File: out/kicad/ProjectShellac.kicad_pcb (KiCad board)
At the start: 4 copper layers, 220 x 140 mm, 259 parts, among them U101 OPA1656, U103 OPA1655, U201 OPA1656, U203 OPA1655, U3001 OPA1612, U3501 OPA1612, U401 OPA1656, U501 OPA1656, U700 OPA1656, U750 OPA1656, U8001 L THAT1646, U9001 R THAT1646

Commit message: AE-074: migrate DR-039 branch-local DC block and reconcile native PCB
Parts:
- TP3004: value L_EQ_RAW -> L_RECOVERY_OUT
- TP3005: value L_EQ_OUT -> L_POST_EQ
- TP3504: value R_EQ_RAW -> R_RECOVERY_OUT
- TP3505: value R_EQ_OUT -> R_POST_EQ
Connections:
- C30060 pad 1: Net-(TP3004-TP) -> Net-(C30060-Pad1)
- C35060 pad 1: Net-(TP3504-TP) -> Net-(C35060-Pad1)
- R30041 pad 1: Net-(TP3004-TP) -> ROOT__POST_EQ_L
- R30060 pad 1: ROOT__POST_EQ_L -> Net-(C30060-Pad1)
- R35041 pad 1: Net-(TP3504-TP) -> ROOT__POST_EQ_R
- R35060 pad 1: ROOT__POST_EQ_R -> Net-(C35060-Pad1)
- TP3004 pad 1: Net-(TP3004-TP) -> ROOT__POST_EQ_L
- TP3504 pad 1: Net-(TP3504-TP) -> ROOT__POST_EQ_R
- U3001 pad 7: Net-(TP3004-TP) -> ROOT__POST_EQ_L
- U3501 pad 7: Net-(TP3504-TP) -> ROOT__POST_EQ_R

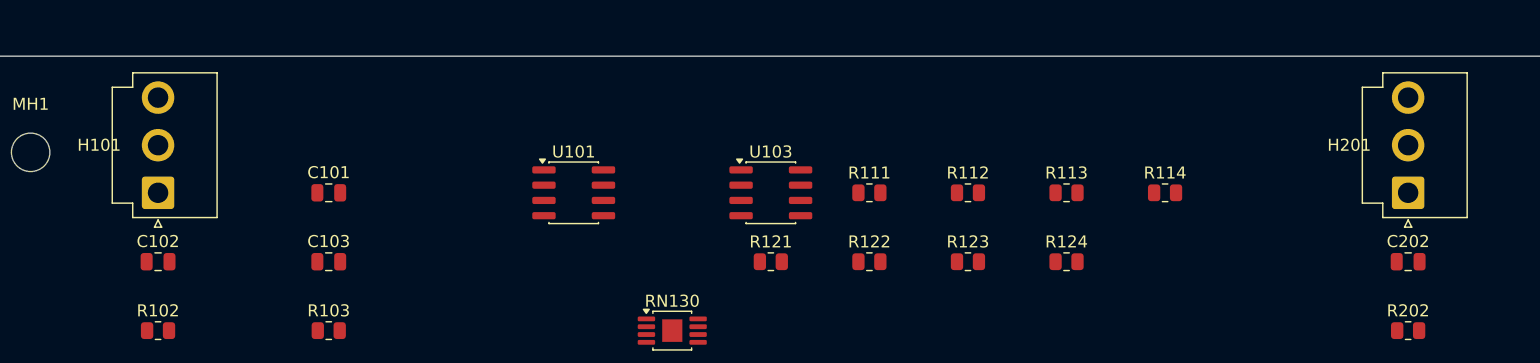
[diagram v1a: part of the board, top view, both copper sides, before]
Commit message: AE-075: close B07 cartridge input harness and Micro-Lock migration
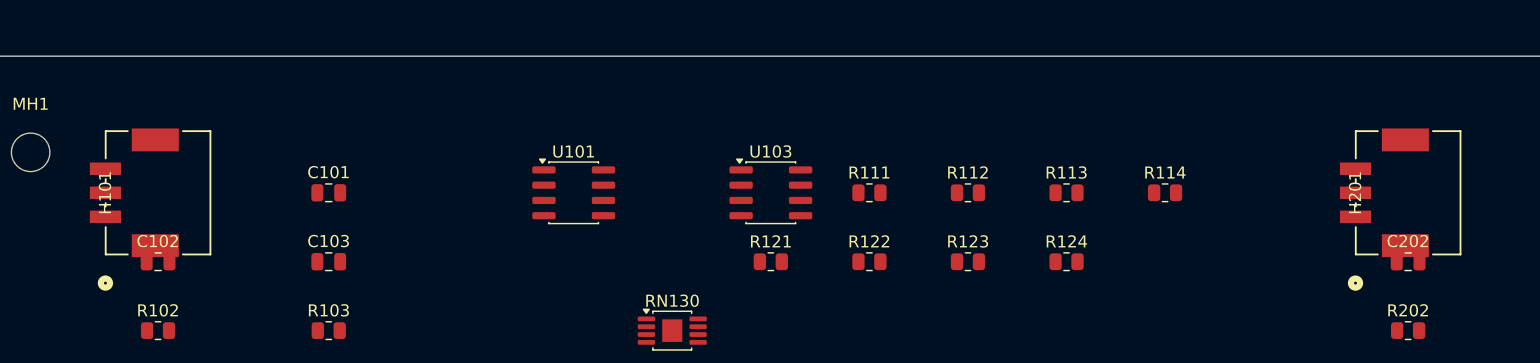
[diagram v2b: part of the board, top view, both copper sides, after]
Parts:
- H101, H201: footprint Connector_JST:JST_VH_B3P-VH_1x03_P3.96mm_Vertical -> ProjectShellac:Molex_MicroLockPlus_5055780321_1x03_P2.00mm_Horizontal

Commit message: AE-075A: reconcile post-SR043 placement and close B05 sense capacitor
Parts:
- C80010, C80011, C90010, C90011: footprint Capacitor_THT:C_Radial_D5.0mm_H5.0mm_P2.00mm -> ProjectShellac:Panasonic_ECEA1VN100U_D5.0mm_H11.0mm_P2.00mm
- moved H121 219.9 mm to (220.4, 32.1), turned to 90 degrees
- moved H120 209.6 mm to (209.2, 32.1), turned to 90 degrees
- moved H122 208.7 mm to (209.2, 39.3), turned to 90 degrees
- moved R4502 200.5 mm to (209.7, 97.3)
- moved R4002 194.2 mm to (200.9, 97.3)
- moved TP506 187.4 mm to (185.7, 116.2)
- moved H111 168.8 mm to (182.2, 32.1)
- moved H110 164.8 mm to (171.0, 32.1)
- moved H112 152.4 mm to (171.0, 39.3)
- moved C293 141.7 mm to (154.7, 32.0)
- moved C292 137.5 mm to (150.3, 32.0)
- moved C291 133.5 mm to (145.9, 32.0)
- moved C294 110.7 mm to (123.3, 37.9)
- moved C204 93.6 mm to (103.4, 38.4)
- moved R205 88.0 mm to (103.4, 42.0)
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
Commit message: AE-075B: reconcile XLR LT5400 service hardware and authority debt
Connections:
- RN130 pad 9: unconnected-(RN130-EP-Pad9) -> 0VA
- RN230 pad 9: unconnected-(RN230-EP-Pad9) -> 0VA
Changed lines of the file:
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@@
 	(net 84 "Net-(R70090-Pad2)")
 	(net 85 "Net-(R75090-Pad2)")
-	(net 86 "unconnected-(RN130-EP-Pad9)")
 	(net 87 "ROOT__PRE_EQ_L")
 	(net 88 "/SCH101 Balanced Input and Differential Conversion/SCH101_L_LT5400_MINUS_SUM")
@@
 	(net 91 "/SCH101 Balanced Input and Differential Conversion/SCH101_R_LT5400_MINUS_SUM")
 	(net 92 "ROOT__PRE_EQ_R")
-	(net 93 "unconnected-(RN230-EP-Pad9)")
 	(net 94 "Net-(U700B-IN)")
 	(net 95 "ROOT__FILTERED_L")
@@
 			)
 		)
-		(property "EP" "Pin 9 presently floating; final EP disposition open"
+		(property "EP" "Pin 9 bonded to quiet 0VA per ADI LT5400 exposed-pad guidance"
 			(at 0 0 0)
 			(unlocked yes)
@@
 			)
 		)
-		(property "Grade" "B-grade procurement candidate; RUN10 acceptance open"
+		(property "Grade" "LT5400BIMS8E-7#PBF selected; B grade; RUN10 full-stage acceptance open"
 			(at 0 0 0)
 			(unlocked yes)
@@
 			(property pad_prop_heatsink)
 			(layers "F.Cu" "F.Mask")
-			(net 86 "unconnected-(RN130-EP-Pad9)")
+			(net 4 "0VA")
 			(pinfunction "EP")
-			(pintype "passive+no_connect")
+			(pintype "passive")
 			(zone_connect 2)
 		)
@@
 			)
 		)
-		(property "EP" "Pin 9 presently floating; final EP disposition open"
+		(property "EP" "Pin 9 bonded to quiet 0VA per ADI LT5400 exposed-pad guidance"
 			(at 0 0 0)
 			(unlocked yes)
@@
 			)
 		)
-		(property "Grade" "B-grade procurement candidate; RUN10 acceptance open"
+		(property "Grade" "LT5400BIMS8E-7#PBF selected; B grade; RUN10 full-stage acceptance open"
 			(at 0 0 0)
 			(unlocked yes)
@@
 			(property pad_prop_heatsink)
 			(layers "F.Cu" "F.Mask")
-			(net 93 "unconnected-(RN230-EP-Pad9)")
+			(net 4 "0VA")
 			(pinfunction "EP")
-			(pintype "passive+no_connect")
+			(pintype "passive")
 			(zone_connect 2)
 		)

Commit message: AE-075G: reconcile output interface and PRE90 evidence
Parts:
- added H801: L OUTPUT HARNESS, ProjectShellac:Molex_MicroLockPlus_5055780221_1x02_P2.00mm_Horizontal, F.Cu at (140.1, 105.8)
- added H802: R OUTPUT HARNESS, ProjectShellac:Molex_MicroLockPlus_5055780221_1x02_P2.00mm_Horizontal, F.Cu at (140.1, 117.7)

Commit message: AE-076A: establish 17 V rail authority and requalify output
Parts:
- TP901: value +18VA_IN -> +17VA_IN
- TP903: value -18VA_IN -> -17VA_IN
- TP9901: value +18V_LED_DRIVE -> +17V_LED_DRIVE
- TP9902: value -18V_LED_DRIVE -> -17V_LED_DRIVE
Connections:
- net +18V renamed +17V
- net -18V renamed -17V
- net /SCH106 Audio-Box Power Entry and Ground Bond/+18VA_IN renamed /SCH106 Audio-Box Power Entry and Ground Bond/+17VA_IN
- net /SCH106 Audio-Box Power Entry and Ground Bond/-18VA_IN renamed /SCH106 Audio-Box Power Entry and Ground Bond/-17VA_IN

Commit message: AE-076E-B: reconcile native personality interface and STEP model authority
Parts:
- removed C103, C203: 47p, Capacitor_SMD:C_0805_2012Metric
- removed C104, C204: 100p, Capacitor_SMD:C_0805_2012Metric
- removed H121: LOAD BASE / PARK, Connector_PinHeader_2.54mm:PinHeader_2x02_P2.54mm_Vertical
- removed H122: LOAD +100p L/R, Connector_PinHeader_2.54mm:PinHeader_2x02_P2.54mm_Vertical
- added H220: R LOAD PERSONALITY, ProjectShellac:Samtec_SLW-102-01-G-D_2x02_P2.54mm_Vertical, F.Cu at (220.4, 32.1)
- H120: value LOAD +47p L/R -> L LOAD PERSONALITY; footprint Connector_PinHeader_2.54mm:PinHeader_2x02_P2.54mm_Vertical -> ProjectShellac:Samtec_SLW-102-01-G-D_2x02_P2.54mm_Vertical
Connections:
- H120 pad 1: /SCH101 Balanced Input and Differential Conversion/SCH101_L_LOAD47_BRANCH -> /SCH101 Balanced Input and Differential Conversion/SCH101_L_LOAD_POS
- H120 pad 3: /SCH101 Balanced Input and Differential Conversion/SCH101_R_LOAD47_BRANCH -> /SCH101 Balanced Input and Differential Conversion/SCH101_L_LOAD_NEG
- H120 pad 4: /SCH101 Balanced Input and Differential Conversion/SCH101_R_LOAD_NEG -> /SCH101 Balanced Input and Differential Conversion/SCH101_L_LOAD_POS
